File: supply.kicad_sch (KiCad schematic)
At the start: 71 parts, among them U1 AP7330-W5-7, U2 AP7330-W5-7, U3 AP7330-W5-7, U4 AP62301WU-7, U5 AP62301WU-7, U6 AP62301WU-7

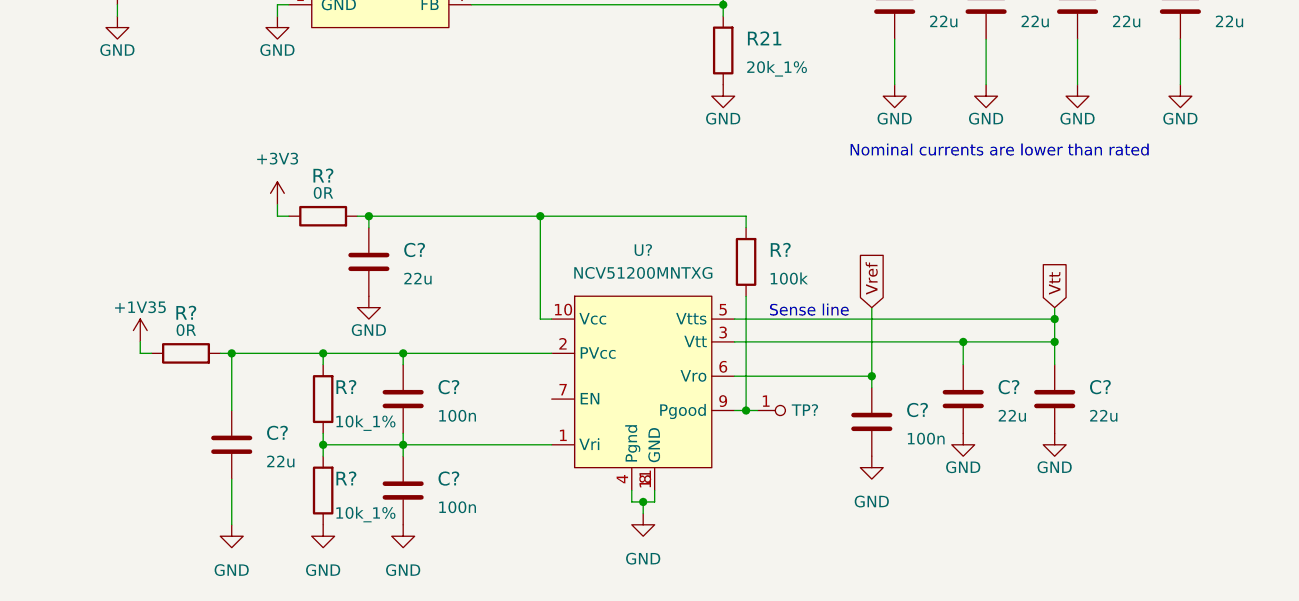
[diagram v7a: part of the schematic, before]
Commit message: Made a connection between DDR3 and fpga on the schematic
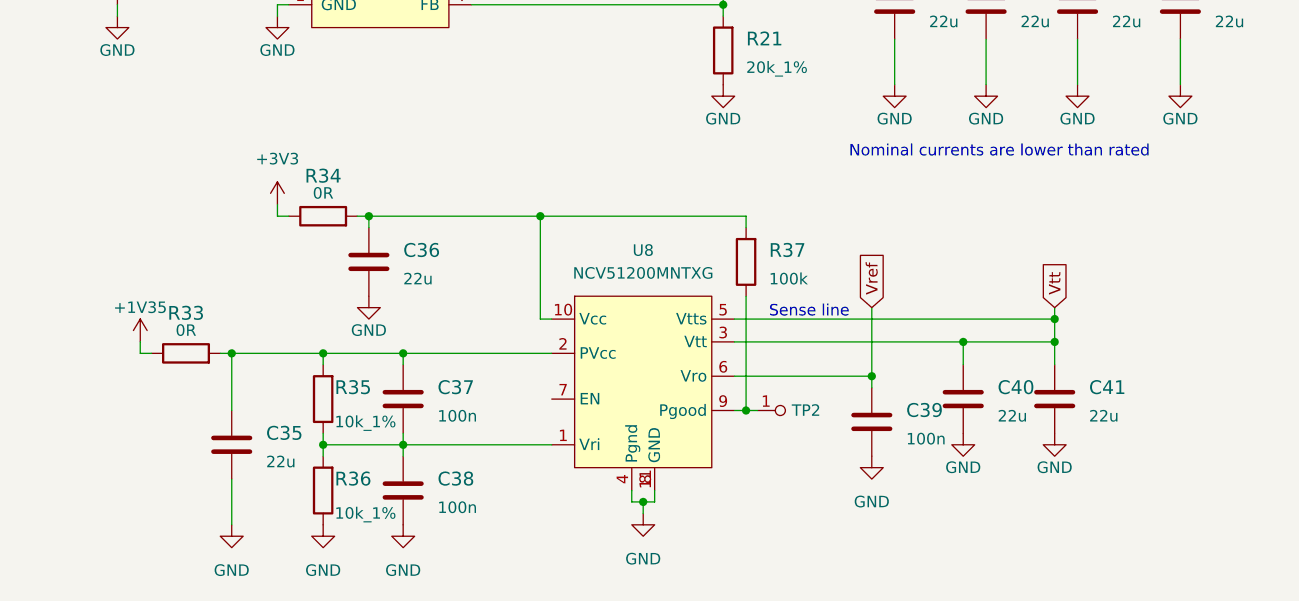
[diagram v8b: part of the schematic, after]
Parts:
- gave numbers to parts that had none: 14
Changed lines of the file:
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@@
   (symbol (lib_id "antmicroCapacitors0402:C_100n_0402") (at 118.11 167.64 0) (unit 1)
     (in_bom yes) (on_board yes) (fields_autoplaced)
-    (property "Reference" "C?" (id 0) (at 121.92 166.37 0)
+    (property "Reference" "C39" (id 0) (at 121.92 166.37 0)
       (effects (font (size 1.524 1.524)) (justify left))
     )
@@
   (symbol (lib_id "antmicroPMICVoltageRegulatorsLinear:NCV51200MNTXG") (at 92.71 163.83 0) (unit 1)
     (in_bom yes) (on_board yes) (fields_autoplaced)
-    (property "Reference" "U?" (id 0) (at 92.71 148.59 0))
+    (property "Reference" "U8" (id 0) (at 92.71 148.59 0))
     (property "Value" "NCV51200MNTXG" (id 1) (at 92.71 151.13 0))
     (property "Footprint" "antmicro-footprints:DFN-10-1EP_3x3mm" (id 2) (at 95.25 187.96 0)
@@
   (symbol (lib_id "power:GND") (at 128.27 168.91 0) (unit 1)
     (in_bom yes) (on_board yes)
-    (property "Reference" "#PWR?" (id 0) (at 128.27 175.26 0)
+    (property "Reference" "#PWR0167" (id 0) (at 128.27 175.26 0)
       (effects (font (size 1.27 1.27)) hide)
     )
@@
   (symbol (lib_id "antmicroCapacitors0402:C_100n_0402") (at 66.04 175.26 0) (unit 1)
     (in_bom yes) (on_board yes) (fields_autoplaced)
-    (property "Reference" "C?" (id 0) (at 69.85 173.99 0)
+    (property "Reference" "C38" (id 0) (at 69.85 173.99 0)
       (effects (font (size 1.524 1.524)) (justify left))
     )
@@
   (symbol (lib_id "power:+3V3") (at 52.07 143.51 0) (unit 1)
     (in_bom yes) (on_board yes) (fields_autoplaced)
-    (property "Reference" "#PWR?" (id 0) (at 52.07 147.32 0)
+    (property "Reference" "#PWR0164" (id 0) (at 52.07 147.32 0)
       (effects (font (size 1.27 1.27)) hide)
     )
@@
   (symbol (lib_id "antmicroCapacitors0402:C_100n_0402") (at 66.04 165.1 0) (unit 1)
     (in_bom yes) (on_board yes) (fields_autoplaced)
-    (property "Reference" "C?" (id 0) (at 69.85 163.83 0)
+    (property "Reference" "C37" (id 0) (at 69.85 163.83 0)
       (effects (font (size 1.524 1.524)) (justify left))
     )
@@
   (symbol (lib_id "power:GND") (at 92.71 177.8 0) (unit 1)
     (in_bom yes) (on_board yes) (fields_autoplaced)
-    (property "Reference" "#PWR?" (id 0) (at 92.71 184.15 0)
+    (property "Reference" "#PWR0165" (id 0) (at 92.71 184.15 0)
       (effects (font (size 1.27 1.27)) hide)
     )
@@
   (symbol (lib_id "power:GND") (at 138.43 168.91 0) (unit 1)
     (in_bom yes) (on_board yes)
-    (property "Reference" "#PWR?" (id 0) (at 138.43 175.26 0)
+    (property "Reference" "#PWR0166" (id 0) (at 138.43 175.26 0)
       (effects (font (size 1.27 1.27)) hide)
     )
@@
   (symbol (lib_id "power:GND") (at 57.15 179.07 0) (unit 1)
     (in_bom yes) (on_board yes) (fields_autoplaced)
-    (property "Reference" "#PWR?" (id 0) (at 57.15 185.42 0)
+    (property "Reference" "#PWR0161" (id 0) (at 57.15 185.42 0)
       (effects (font (size 1.27 1.27)) hide)
     )
@@
   (symbol (lib_id "power:GND") (at 118.11 171.45 0) (unit 1)
     (in_bom yes) (on_board yes) (fields_autoplaced)
-    (property "Reference" "#PWR?" (id 0) (at 118.11 177.8 0)
+    (property "Reference" "#PWR0168" (id 0) (at 118.11 177.8 0)
       (effects (font (size 1.27 1.27)) hide)
     )
@@
   (symbol (lib_id "antmicroResistors0603:R_10k_1%_0603") (at 57.15 165.1 90) (unit 1)
     (in_bom yes) (on_board yes)
-    (property "Reference" "R?" (id 0) (at 58.42 163.83 90)
+    (property "Reference" "R35" (id 0) (at 58.42 163.83 90)
       (effects (font (size 1.524 1.524)) (justify right))
     )
@@
   (symbol (lib_id "antmicroCapacitorsmisc:C_22u_0805") (at 46.99 170.18 0) (unit 1)
     (in_bom yes) (on_board yes) (fields_autoplaced)
-    (property "Reference" "C?" (id 0) (at 50.8 168.91 0)
+    (property "Reference" "C35" (id 0) (at 50.8 168.91 0)
       (effects (font (size 1.524 1.524)) (justify left))
     )
@@
   (symbol (lib_id "power:GND") (at 46.99 179.07 0) (unit 1)
     (in_bom yes) (on_board yes) (fields_autoplaced)
-    (property "Reference" "#PWR?" (id 0) (at 46.99 185.42 0)
+    (property "Reference" "#PWR0158" (id 0) (at 46.99 185.42 0)
       (effects (font (size 1.27 1.27)) hide)
     )
@@
   (symbol (lib_id "antmicroResistorsmisc:R_0R_0805") (at 41.91 160.02 0) (unit 1)
     (in_bom yes) (on_board yes)
-    (property "Reference" "R?" (id 0) (at 41.91 155.575 0)
+    (property "Reference" "R33" (id 0) (at 41.91 155.575 0)
       (effects (font (size 1.524 1.524)))
     )
@@
   (symbol (lib_id "antmicroCapacitorsmisc:C_22u_0805") (at 138.43 165.1 0) (unit 1)
     (in_bom yes) (on_board yes) (fields_autoplaced)
-    (property "Reference" "C?" (id 0) (at 142.24 163.83 0)
+    (property "Reference" "C41" (id 0) (at 142.24 163.83 0)
       (effects (font (size 1.524 1.524)) (justify left))
     )
@@
   (symbol (lib_id "antmicroTestPoints:TP") (at 107.95 166.37 90) (unit 1)
     (in_bom yes) (on_board yes) (fields_autoplaced)
-    (property "Reference" "TP?" (id 0) (at 109.22 166.3699 90)
+    (property "Reference" "TP2" (id 0) (at 109.22 166.3699 90)
       (effects (font (size 1.27 1.27)) (justify right))
     )
@@
   (symbol (lib_id "antmicroResistorsmisc:R_0R_0805") (at 57.15 144.78 0) (unit 1)
     (in_bom yes) (on_board yes)
-    (property "Reference" "R?" (id 0) (at 57.15 140.335 0)
+    (property "Reference" "R34" (id 0) (at 57.15 140.335 0)
       (effects (font (size 1.524 1.524)))
     )
@@
   (symbol (lib_id "power:GND") (at 62.23 153.67 0) (unit 1)
     (in_bom yes) (on_board yes)
-    (property "Reference" "#PWR?" (id 0) (at 62.23 160.02 0)
+    (property "Reference" "#PWR0159" (id 0) (at 62.23 160.02 0)
       (effects (font (size 1.27 1.27)) hide)
     )
@@
   (symbol (lib_id "antmicroCapacitorsmisc:C_22u_0805") (at 62.23 149.86 0) (unit 1)
     (in_bom yes) (on_board yes) (fields_autoplaced)
-    (property "Reference" "C?" (id 0) (at 66.04 148.59 0)
+    (property "Reference" "C36" (id 0) (at 66.04 148.59 0)
       (effects (font (size 1.524 1.524)) (justify left))
     )
@@
   (symbol (lib_id "power:GND") (at 66.04 179.07 0) (unit 1)
     (in_bom yes) (on_board yes) (fields_autoplaced)
-    (property "Reference" "#PWR?" (id 0) (at 66.04 185.42 0)
+    (property "Reference" "#PWR0162" (id 0) (at 66.04 185.42 0)
       (effects (font (size 1.27 1.27)) hide)
     )
@@
   (symbol (lib_id "antmicroResistors0603:R_100k_0603") (at 104.14 149.86 90) (unit 1)
     (in_bom yes) (on_board yes) (fields_autoplaced)
-    (property "Reference" "R?" (id 0) (at 106.68 148.59 90)
+    (property "Reference" "R37" (id 0) (at 106.68 148.59 90)
       (effects (font (size 1.524 1.524)) (justify right))
     )
@@
   (symbol (lib_id "antmicroCapacitorsmisc:C_22u_0805") (at 128.27 165.1 0) (unit 1)
     (in_bom yes) (on_board yes) (fields_autoplaced)
-    (property "Reference" "C?" (id 0) (at 132.08 163.83 0)
+    (property "Reference" "C40" (id 0) (at 132.08 163.83 0)
       (effects (font (size 1.524 1.524)) (justify left))
     )
@@
   (symbol (lib_id "power:+1V35") (at 36.83 158.75 0) (unit 1)
     (in_bom yes) (on_board yes)
-    (property "Reference" "#PWR?" (id 0) (at 36.83 162.56 0)
+    (property "Reference" "#PWR0163" (id 0) (at 36.83 162.56 0)
       (effects (font (size 1.27 1.27)) hide)
     )
@@
   (symbol (lib_id "antmicroResistors0603:R_10k_1%_0603") (at 57.15 175.26 90) (unit 1)
     (in_bom yes) (on_board yes)
-    (property "Reference" "R?" (id 0) (at 58.42 173.99 90)
+    (property "Reference" "R36" (id 0) (at 58.42 173.99 90)
       (effects (font (size 1.524 1.524)) (justify right))
     )
